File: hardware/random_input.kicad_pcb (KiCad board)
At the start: 2 copper layers, 47 x 36.8 mm, 28 parts, among them J1 FS, J2 FS_G, J3 In_G, J4 Out_G, J5 -, J6 In, J7 Out, J8 +, Q1 NPN Ge, Q2 NPN Ge

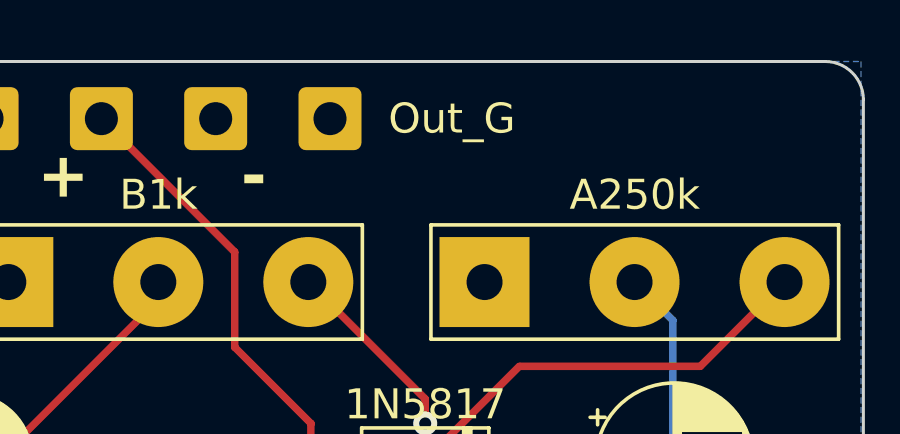
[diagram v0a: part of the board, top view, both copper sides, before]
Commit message: mostly cosmetic updates
 - add copper finish
 - move revision and web reference to a global variable
 - minor text updates
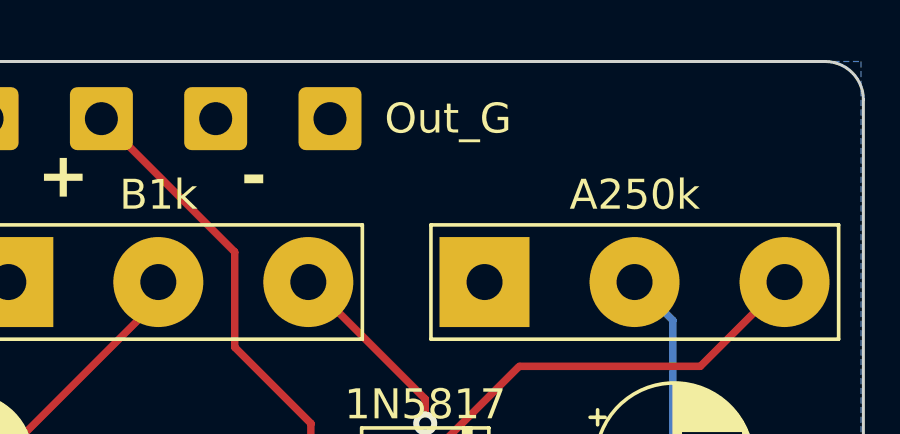
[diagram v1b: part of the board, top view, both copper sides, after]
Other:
- board text added: "${COMMENT1}"
- board text added: "${REVISION}"
- board text removed: "github.com/whbeers/random_input"
- board text removed: "v0.01"
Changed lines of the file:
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@@
   )
   (paper "A4")
+  (title_block
+    (title "Random Input Fuzz Effect")
+    (date "2023-02-22")
+    (rev "v0.01")
+    (comment 1 " github.com/whbeers/random_input")
+  )
   (layers
     (0 "F.Cu" signal)
-    (31 "B.Cu" signal)
+    (31 "B.Cu" power)
     (33 "F.Adhes" user "F.Adhesive")
     (36 "B.SilkS" user "B.Silkscreen")
@@
       (layer "B.Mask" (type "Bottom Solder Mask") (thickness 0.01))
       (layer "B.SilkS" (type "Bottom Silk Screen"))
-      (copper_finish "None")
+      (copper_finish "HAL SnPb")
       (dielectric_constraints no)
     )
@@
         (effects (font (size 1 1) (thickness 0.15)))
     )
-    (fp_text value "Out_G" (at 4.064 0) (layer "F.SilkS" knockout)
+    (fp_text value "Out_G" (at 3.937 0) (layer "F.SilkS" knockout)
         (effects (font (size 1 1) (thickness 0.15)))
     )
@@
   (gr_line (start 71.12 22.86) (end 71.12 57.15)
     (stroke (width 0.1) (type default)) (layer "Edge.Cuts"))
-  (gr_text "v0.01" (at 27.94 58.166) (layer "B.SilkS" knockout)
+  (gr_text "${REVISION}" (at 27.94 58.166) (layer "B.SilkS" knockout)
     (effects (font (size 0.8 0.8) (thickness 0.15)) (justify left bottom mirror))
   )
-  (gr_text " github.com/whbeers/random_input" (at 70.866 58.166) (layer "B.SilkS" knockout)
+  (gr_text "${COMMENT1}" (at 70.866 58.166) (layer "B.SilkS" knockout)
     (effects (font (size 0.8 0.8) (thickness 0.15)) (justify left bottom mirror))
   )

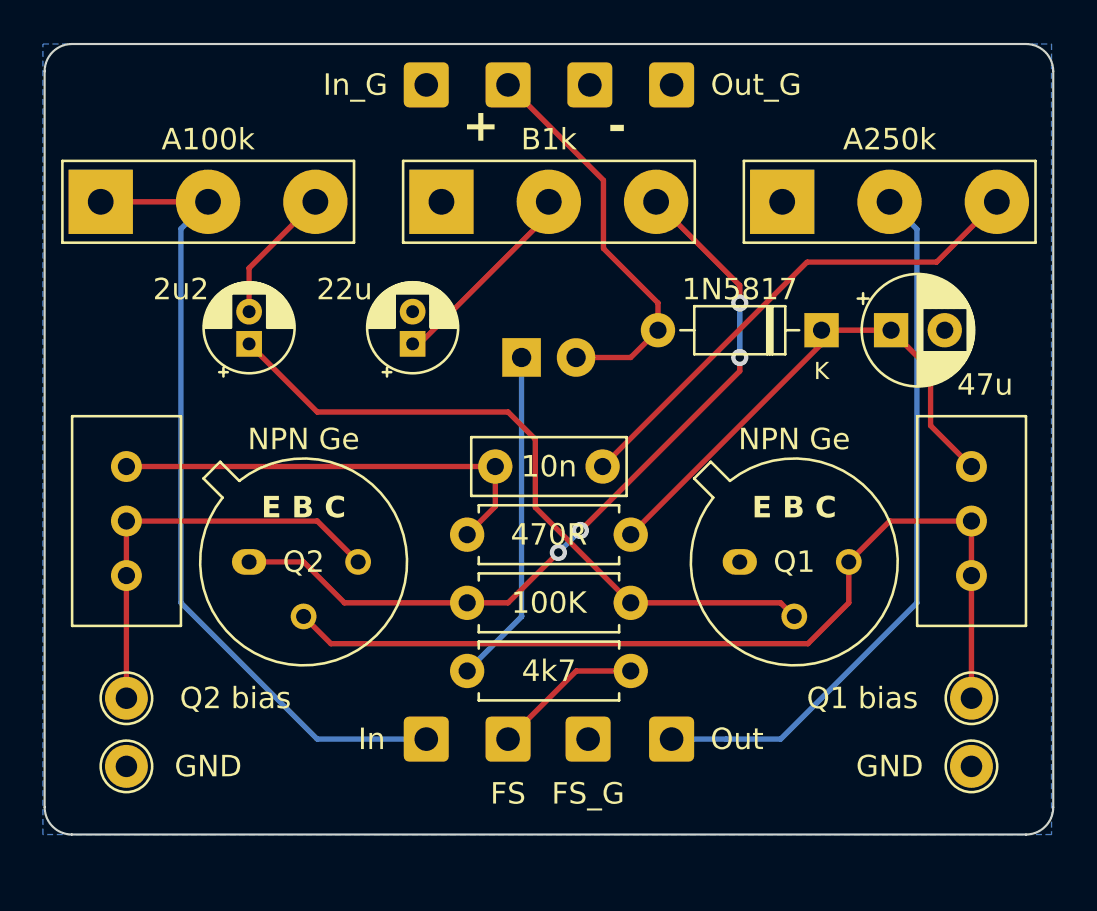
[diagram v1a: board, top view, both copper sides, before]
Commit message: Address issues found in v0.01 hardware
 - Move all potentiometers to back copper layer (they were reversed)
 - cosmetic/usability updates
 - adjust value of Q2 trimpot to allow correct biasing
 - swap FS and FS_G wires
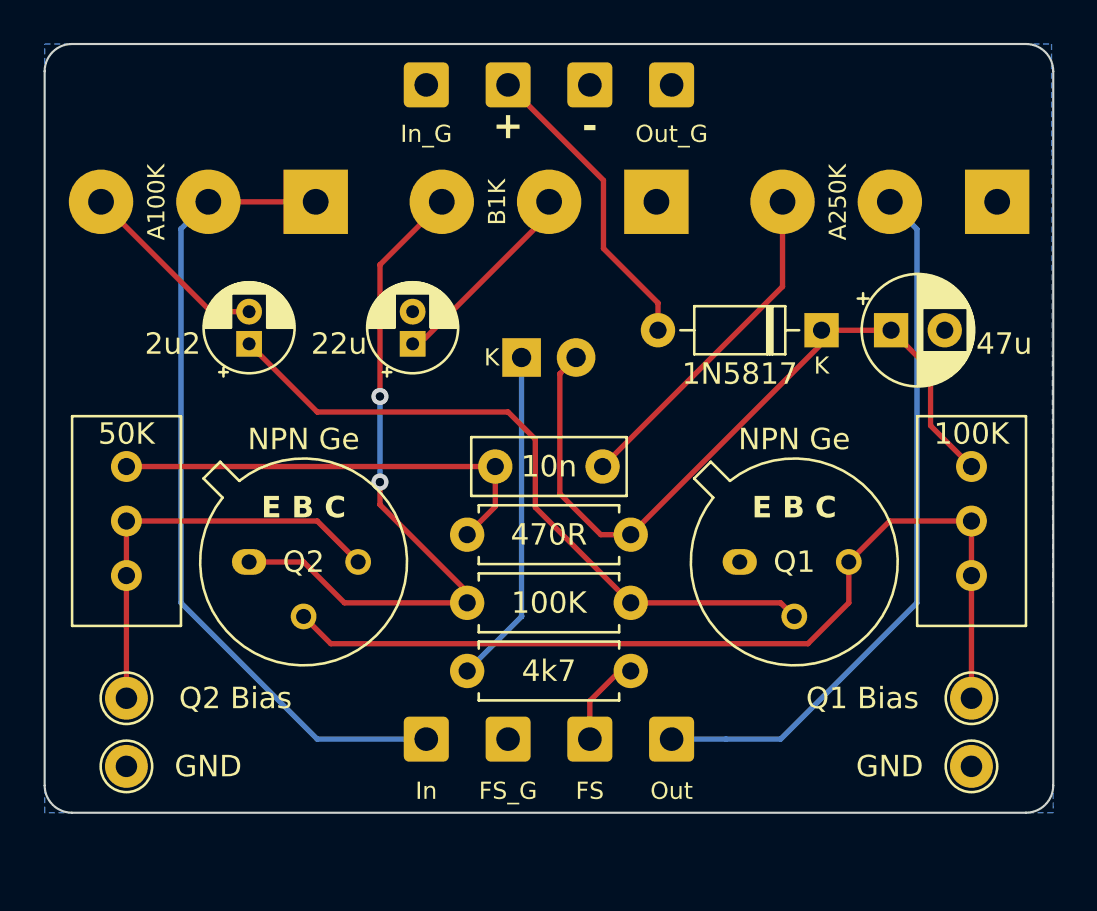
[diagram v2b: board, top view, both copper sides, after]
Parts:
- POT1: value Input Volume -> A100K; moved to B.Cu
- POT2: value Fuzz -> B1K; moved to B.Cu
- POT3: value Volume -> A250K; moved to B.Cu
- TP1: value Q1 bias -> Q1 Bias
- TP2: value Q2 bias -> Q2 Bias
- TRIM1: value Q1_BIAS_100K -> 100K
- TRIM2: value Q2_BIAS_20K -> 50K
- moved J1 3.81 mm to (49.5, 54.0)
- moved J2 3.73 mm to (45.7, 54.0)
- turned POT1 to 180 degrees
- turned POT2 to 180 degrees
- turned POT3 to 180 degrees
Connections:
- D2 pad 2: /DC_SHIELD -> 9V
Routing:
- net 9V: track 24.3 -> 35.1 mm
- net /PRE_VOLUME: track 23.4 -> 15.8 mm
- net /Q2_E: track 37.6 -> 32.5 mm, vias 4 -> 2
- net /DC_SHIELD: track 18.7 -> 14.3 mm
- net /Footswitch: track 7.03 -> 4.26 mm
- net Net-(C2-Pad2): track 6.40 -> 9.02 mm
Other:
- board size 47 x 36.8 mm -> 47 x 35.8 mm

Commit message: Updates for v0.2:
 - Switch from wire connectors to molex picoblade connectors
 - Increase size / ergonomics of bias testing pads to suit more probe types
 - Various cosmetic fixes
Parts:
- removed J3: In_G, Connector_Wire:SolderWire-0.5sqmm_1x01_D0.9mm_OD2.1mm
- removed J4: Out_G, Connector_Wire:SolderWire-0.5sqmm_1x01_D0.9mm_OD2.1mm
- removed J5: -, Connector_Wire:SolderWire-0.5sqmm_1x01_D0.9mm_OD2.1mm
- removed J6: In, Connector_Wire:SolderWire-0.5sqmm_1x01_D0.9mm_OD2.1mm
- removed J7: Out, Connector_Wire:SolderWire-0.5sqmm_1x01_D0.9mm_OD2.1mm
- removed J8: +, Connector_Wire:SolderWire-0.5sqmm_1x01_D0.9mm_OD2.1mm
- J1: value FS -> Upper Connector; footprint Connector_Wire:SolderWire-0.5sqmm_1x01_D0.9mm_OD2.1mm -> Connector_Molex:Molex_PicoBlade_53047-0410_1x04_P1.25mm_Vertical
- J2: value FS_G -> Upper Connector; footprint Connector_Wire:SolderWire-0.5sqmm_1x01_D0.9mm_OD2.1mm -> Connector_Molex:Molex_PicoBlade_53047-0410_1x04_P1.25mm_Vertical
- TP1, TP2, TP3, TP4: footprint TestPoint:TestPoint_THTPad_D2.0mm_Drill1.0mm -> TestPoint:TestPoint_THTPad_2.5x2.5mm_Drill1.2mm
- moved J1 28.8 mm to (45.9, 25.4)
- moved J2 3.78 mm to (49.5, 54.0), turned to 180 degrees
- moved TP2 2.47 mm to (25.9, 50.7)
- moved TP1 2.47 mm to (69.3, 50.7), turned to -90 degrees
- moved TP4 2.27 mm to (25.9, 54.2)
- moved TP3 2.27 mm to (69.3, 54.2), turned to -90 degrees
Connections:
- J1 pad 1: /Footswitch -> GND
- J2 pad 1: GND -> /OUTPUT_TIP
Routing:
- net /OUTPUT_TIP: track 33.3 -> 37.1 mm
- net /INPUT_TIP: track 38.3 -> 42.1 mm
- net /DC_SHIELD: track 14.3 -> 11.8 mm
- net /Footswitch: track 4.26 -> 4.85 mm
- net /Q2_C: track 19.8 -> 19.3 mm
- net /Q1_C_Q2_B: track 43.4 -> 42.8 mm
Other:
- board size 47 x 35.8 mm -> 47 x 33.1 mm

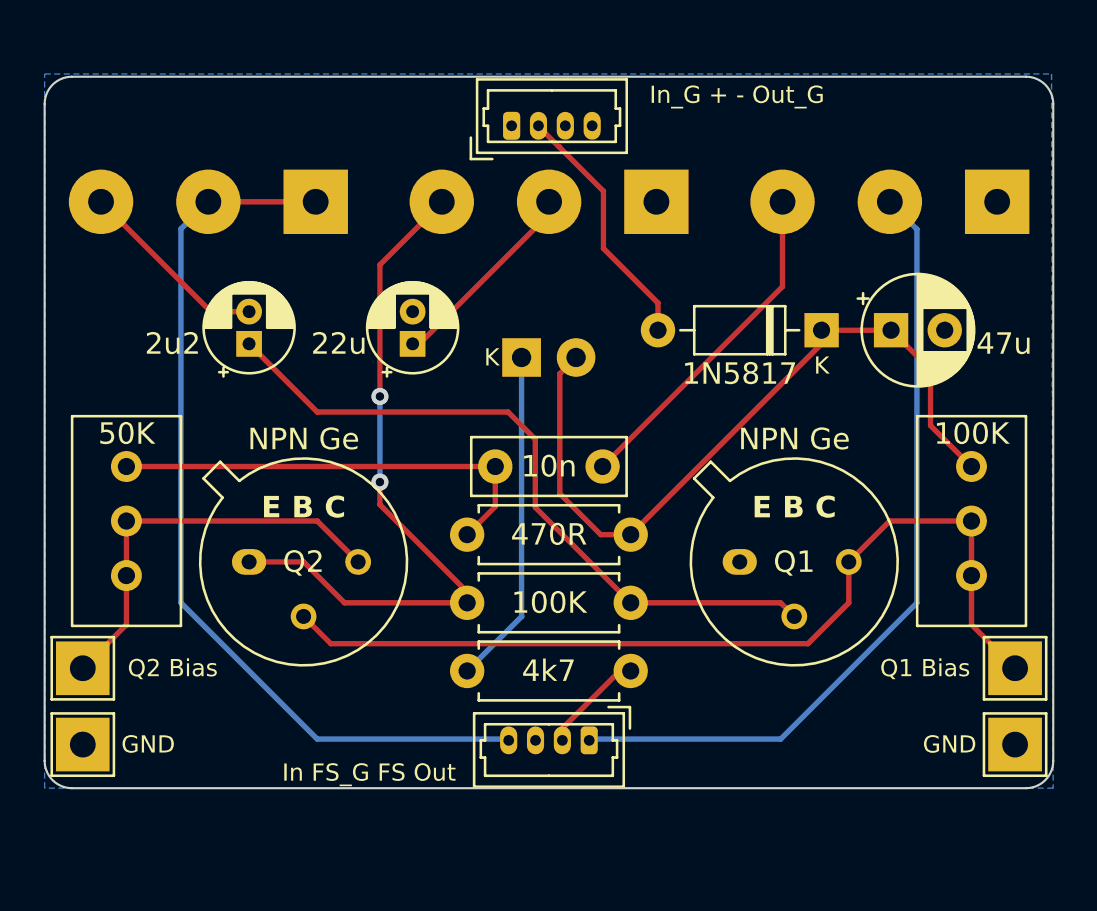
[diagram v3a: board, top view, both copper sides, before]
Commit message: Offload DC protection to "noise floor" utility PCB
 - much rerouting but otherwise functionally the same
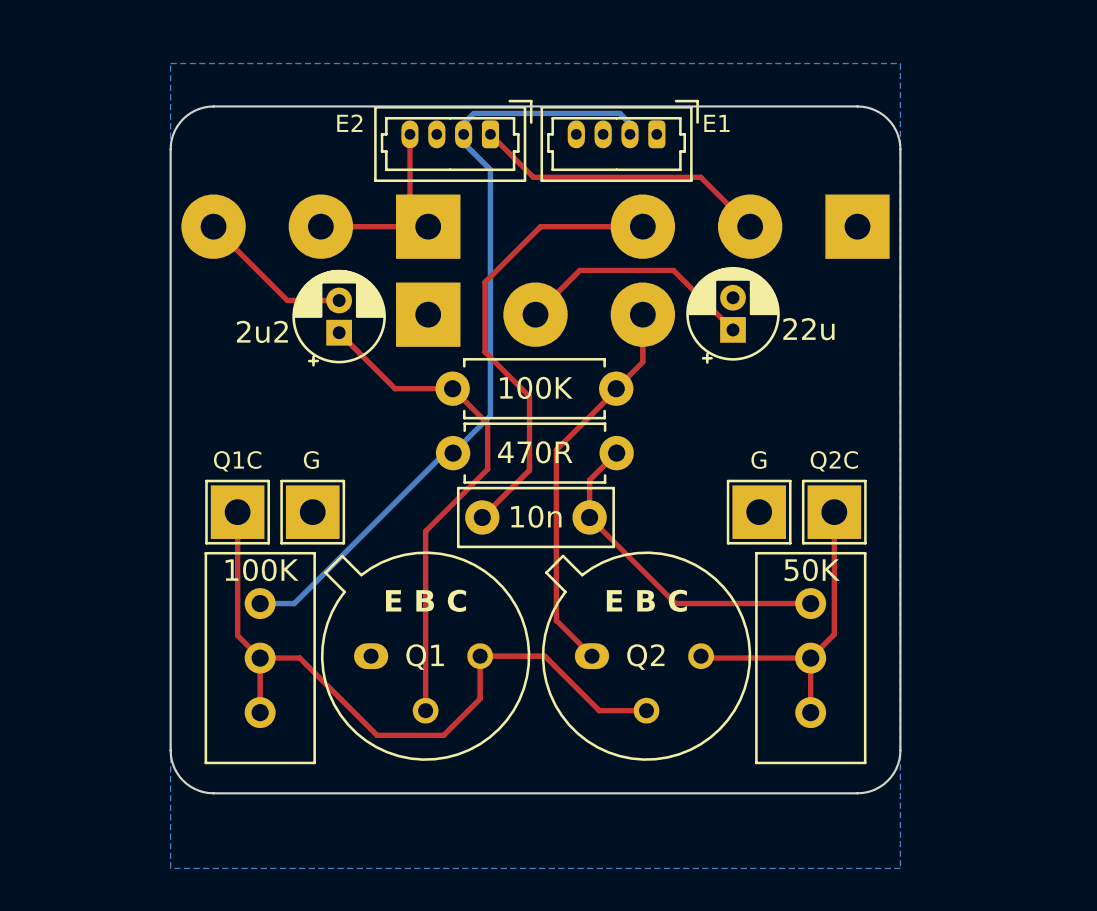
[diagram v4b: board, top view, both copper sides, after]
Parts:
- removed C1: 47u, Capacitor_THT:CP_Radial_D5.0mm_P2.50mm
- removed D1: 1N5817, Diode_THT:D_DO-35_SOD27_P7.62mm_Horizontal
- removed D2: On, LED_THT:LED_D3.0mm
- removed R1: 4k7, Resistor_THT:R_Axial_DIN0207_L6.3mm_D2.5mm_P7.62mm_Horizontal
- J1: value Upper Connector -> E1
- J2: value Upper Connector -> E2
- TP1: value Q1 Bias -> Q1C
- TP2: value Q2 Bias -> Q2C
- TP3, TP4: value GND -> G
- moved TP1 36.9 mm to (33.1, 43.4)
- moved TP2 35.8 mm to (60.9, 43.4)
- moved TRIM1 33.7 mm to (34.2, 47.7)
- moved TRIM2 32.5 mm to (59.8, 47.7)
- moved J2 28.6 mm to (44.9, 25.8)
- moved Q1 17.7 mm to (39.3, 50.1)
- moved Q2 16.6 mm to (49.6, 50.1)
- moved TP3 16.1 mm to (57.4, 43.4)
- moved TP4 15.2 mm to (36.6, 43.4)
- moved C3 14.9 mm to (56.2, 34.9)
- moved R3 13.0 mm to (43.1, 37.6), turned to 0 degrees
- moved POT2 12.9 mm to (47.0, 38.0), turned to 0 degrees
- moved R2 9.11 mm to (43.2, 40.6), turned to 0 degrees
- moved J1 6.77 mm to (52.6, 25.8), turned to 180 degrees
- moved POT3 6.61 mm to (57.0, 26.3)
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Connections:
- net /INPUT_TIP renamed /EFFECT_IN
- net /OUTPUT_TIP renamed /EFFECT_OUT
- J1 pad 1: GND -> unconnected-(J1-Pin_1-Pad1)
- J1 pad 2: /DC_SHIELD -> /9V0
- J1 pad 3: GND -> unconnected-(J1-Pin_3-Pad3)
- J1 pad 4: GND -> unconnected-(J1-Pin_4-Pad4)
- J2 pad 2: /Footswitch -> /9V0
- R2 pad 1: 9V -> /9V0
- TRIM1 pad 1: 9V -> /9V0
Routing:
- net /9V0: track 0.00 -> 37.1 mm
- net 9V: track 35.1 -> 0.00 mm
- net /EFFECT_IN: track 42.1 -> 9.65 mm
- net /EFFECT_OUT: track 37.1 -> 13.9 mm
- net Net-(D2-K): track 15.7 -> 0.00 mm
- net /Q2_E: track 32.5 -> 18.3 mm, vias 2 -> 0
- net /DC_SHIELD: track 11.8 -> 0.00 mm
- net /Q1_C_Q2_B: track 42.8 -> 33.0 mm
- net /Q1_B: track 32.5 -> 23.2 mm
- net /PRE_VOLUME: track 15.8 -> 21.5 mm
- net Net-(C4-Pad1): track 20.9 -> 15.5 mm
- net /Footswitch: track 4.85 -> 0.00 mm
- net /Q2_C: track 19.3 -> 14.9 mm
- net /FUZZ_CTL: track 9.43 -> 11.2 mm
- net Net-(C2-Pad2): track 9.02 -> 7.27 mm
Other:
- board size 47 x 33.1 mm -> 34 x 32 mm

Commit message: Drop to a single connector to simplify, bump rev to v0.26
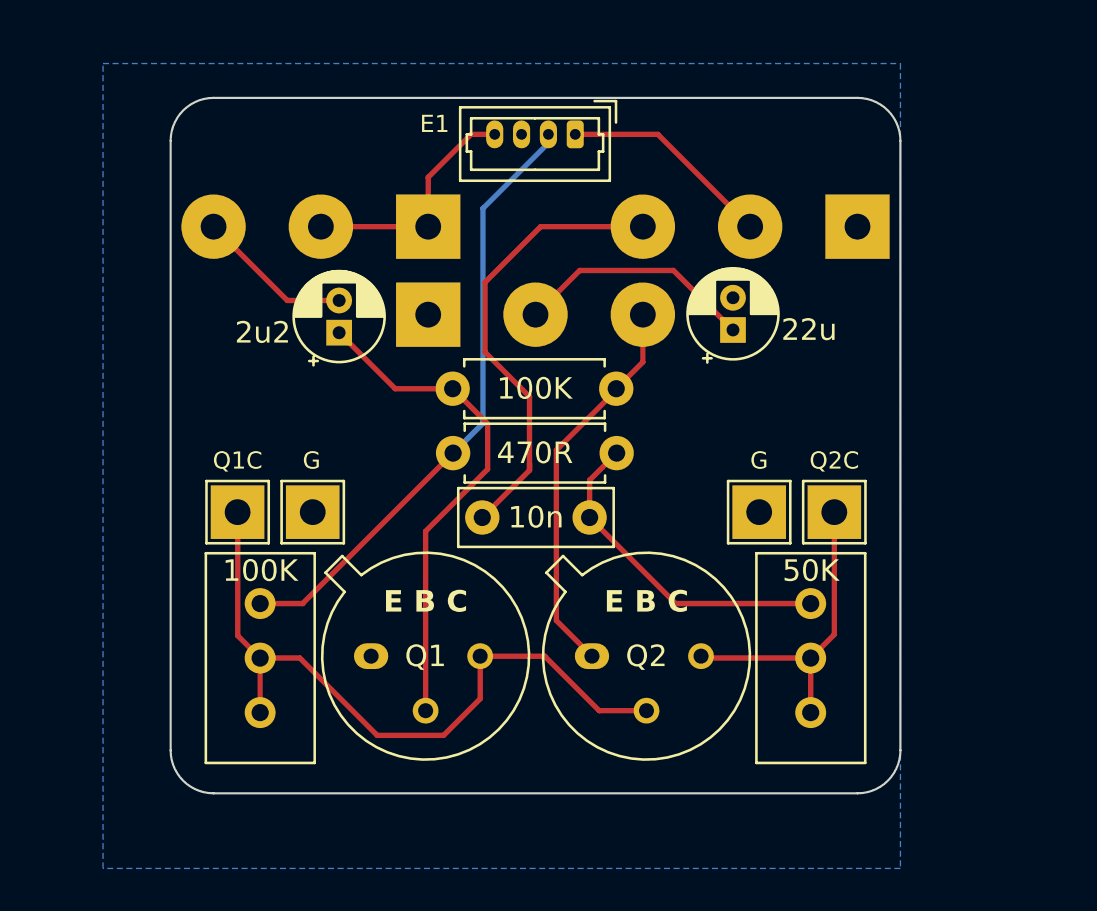
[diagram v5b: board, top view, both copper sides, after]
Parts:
- removed the J1 at (52.6, 25.8)
- J1: renamed from J2; value E2 -> E1
- moved J1 3.95 mm to (48.9, 25.8)
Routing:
- net /9V0: track 37.1 -> 28.6 mm
- net /EFFECT_OUT: track 13.9 -> 9.93 mm
- net /EFFECT_IN: track 9.65 -> 11.2 mm
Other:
- board size 34 x 32 mm -> 34 x 32.4 mm
- board text added: "${COMMENT1} ${REVISION}"
- board text removed: "${COMMENT1}"
- board text removed: "${REVISION}"
